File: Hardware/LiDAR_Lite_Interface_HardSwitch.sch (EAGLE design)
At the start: 40 parts, among them J1 CONN_6SCREW_2.54, J2 CONN_42.54_SCREW, Q1 2N7002, Q2 2N7002, Q3 DMG3404, Q4 MOSFET_PCH-NX2301P, U1 TLV61220DBV, U2 TCS40DPRSOT23, U4 LIS3DHLGA, U5 MIC53653.3SC70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

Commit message: Design updates and gerbers, final DFM required
Added Gerbers for OSH park, naming update, pending v0.2 design
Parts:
- removed Q4: MOSFET_PCH-NX2301P, bschulz:MOSFET_PCH-NX2301P
- added C13: (no value), bschulz_passives:C-EU0.1UFC0603
- added J3: (no value), bschulz:CONN_02
- added JP1: JUMPER-SMT_2_NC_PASTE_SILK, SparkFun-Jumpers:JUMPER-SMT_2_NC_PASTE_SILK
- added R12: 2.2k, bschulz_passives:R-EU_2.2KR0603
- added R13: 1.8k, bschulz_passives:R-EU_1.8KR0603
- added R14: 10k, bschulz_passives:R-EU_10KR0603
- added U7: MIC2544MSOP, bschulz:MIC2544MSOP
- Q1, Q2: value 2N7002 -> MOSFET-NCH-2N7002P
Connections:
- new net FAULT: R14.1, U3.PA5, U7.!FLG
- new net N$5: JP1.1, R12.2, U7.ILIM
- new net N$6: JP1.2, R13.2
- net 5V: now also C13.1, R14.2, U7.IN; no longer Q4.S
- net 5V_SW: now also U7.OUT; no longer Q4.D
- net GND: now also C13.2, J3.1, R12.1, R13.1, U7.GND
- net N$4: now also J3.2
- net POWER_SW: now also U7.EN; no longer Q4.G
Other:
- note added: "Low Current (JP1, OPEN) ~ 100mA High Current (JP1, CLOSED) ~ 230mA"

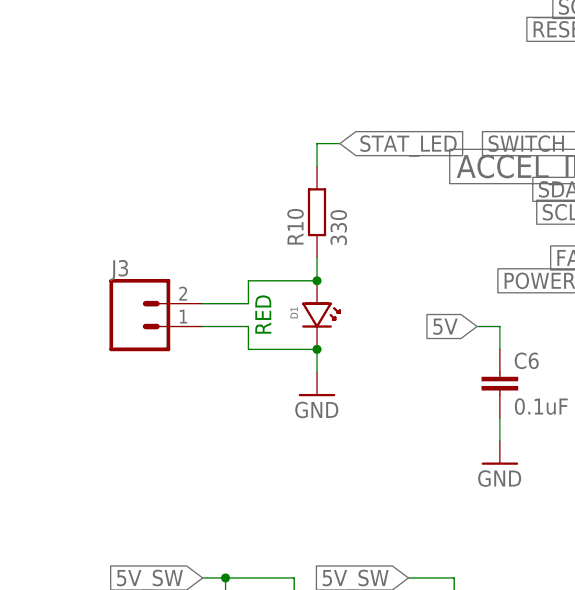
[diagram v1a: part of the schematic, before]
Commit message: Minor edits, changed external LED topology, sent v0.1 to fab
Changed external LED to use independent resistor, generated gerbers, sent v0.1 to fab
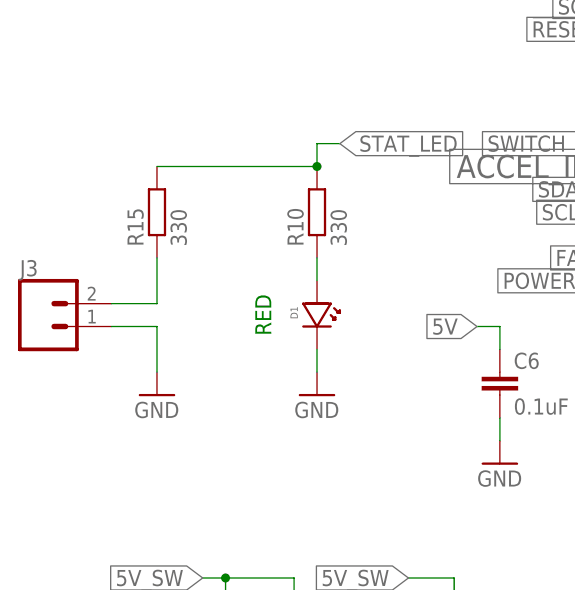
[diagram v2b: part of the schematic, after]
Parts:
- added R15: 330, bschulz_passives:R-EU_330R0603
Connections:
- new net N$2: D1.ANODE, R10.1
- net N$4: now also R15.1; no longer D1.ANODE, R10.1
- net STAT_LED: now also R15.2
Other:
- moved on the sheet: J3
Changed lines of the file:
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@@
 <part name="GND19" library="supply1" library_urn="urn:adsk.eagle:library:371" deviceset="GND" device=""/>
 <part name="J3" library="bschulz" deviceset="CONN_02" device=""/>
+<part name="R15" library="bschulz_passives" deviceset="R-EU_" device="R0603" technology="330" value="330"/>
+<part name="GND21" library="supply1" library_urn="urn:adsk.eagle:library:371" deviceset="GND" device=""/>
 </parts>
 <sheets>
@@
 <attribute name="VALUE" x="271.78" y="-2.54" size="1.778" layer="96"/>
 </instance>
-<instance part="J3" gate="G$1" x="-10.16" y="71.12" smashed="yes">
-<attribute name="VALUE" x="-12.7" y="66.294" size="1.778" layer="96" font="vector"/>
-<attribute name="NAME" x="-12.7" y="76.708" size="1.778" layer="95" font="vector"/>
+<instance part="J3" gate="G$1" x="-20.32" y="71.12" smashed="yes">
+<attribute name="VALUE" x="-22.86" y="66.294" size="1.778" layer="96" font="vector"/>
+<attribute name="NAME" x="-22.86" y="76.708" size="1.778" layer="95" font="vector"/>
+</instance>
+<instance part="R15" gate="G$1" x="-7.62" y="83.82" smashed="yes" rot="R90">
+<attribute name="NAME" x="-9.1186" y="80.01" size="1.778" layer="95" rot="R90"/>
+<attribute name="VALUE" x="-4.318" y="80.01" size="1.778" layer="96" rot="R90"/>
+</instance>
+<instance part="GND21" gate="1" x="-7.62" y="63.5" smashed="yes">
+<attribute name="VALUE" x="-10.16" y="60.96" size="1.778" layer="96"/>
 </instance>
 </instances>
@@
 <wire x1="10.16" y1="68.58" x2="10.16" y2="66.04" width="0.1524" layer="91"/>
 <pinref part="GND20" gate="1" pin="GND"/>
-<pinref part="J3" gate="G$1" pin="1"/>
-<wire x1="-2.54" y1="71.12" x2="2.54" y2="71.12" width="0.1524" layer="91"/>
-<wire x1="2.54" y1="71.12" x2="2.54" y2="68.58" width="0.1524" layer="91"/>
-<wire x1="2.54" y1="68.58" x2="10.16" y2="68.58" width="0.1524" layer="91"/>
-<junction x="10.16" y="68.58"/>
 </segment>
 <segment>
@@
 <wire x1="274.32" y1="2.54" x2="274.32" y2="5.08" width="0.1524" layer="91"/>
 <junction x="274.32" y="5.08"/>
+</segment>
+<segment>
+<pinref part="J3" gate="G$1" pin="1"/>
+<wire x1="-12.7" y1="71.12" x2="-7.62" y2="71.12" width="0.1524" layer="91"/>
+<pinref part="GND21" gate="1" pin="GND"/>
+<wire x1="-7.62" y1="66.04" x2="-7.62" y2="71.12" width="0.1524" layer="91"/>
 </segment>
 </net>
@@
 <net name="N$4" class="0">
 <segment>
-<pinref part="D1" gate="G$1" pin="ANODE"/>
-<pinref part="R10" gate="G$1" pin="1"/>
-<wire x1="10.16" y1="76.2" x2="10.16" y2="78.74" width="0.1524" layer="91"/>
 <pinref part="J3" gate="G$1" pin="2"/>
-<wire x1="-2.54" y1="73.66" x2="2.54" y2="73.66" width="0.1524" layer="91"/>
-<wire x1="2.54" y1="73.66" x2="2.54" y2="76.2" width="0.1524" layer="91"/>
-<wire x1="2.54" y1="76.2" x2="10.16" y2="76.2" width="0.1524" layer="91"/>
-<junction x="10.16" y="76.2"/>
+<wire x1="-12.7" y1="73.66" x2="-7.62" y2="73.66" width="0.1524" layer="91"/>
+<wire x1="-7.62" y1="73.66" x2="-7.62" y2="78.74" width="0.1524" layer="91"/>
+<pinref part="R15" gate="G$1" pin="1"/>
 </segment>
 </net>
@@
 <wire x1="10.16" y1="91.44" x2="12.7" y2="91.44" width="0.1524" layer="91"/>
 <label x="12.7" y="91.44" size="1.778" layer="95" xref="yes"/>
+<pinref part="R15" gate="G$1" pin="2"/>
+<wire x1="10.16" y1="88.9" x2="-7.62" y2="88.9" width="0.1524" layer="91"/>
+<junction x="10.16" y="88.9"/>
 </segment>
 <segment>
@@
 </segment>
 </net>
+<net name="N$2" class="0">
+<segment>
+<pinref part="R10" gate="G$1" pin="1"/>
+<pinref part="D1" gate="G$1" pin="ANODE"/>
+<wire x1="10.16" y1="76.2" x2="10.16" y2="78.74" width="0.1524" layer="91"/>
+</segment>
+</net>
